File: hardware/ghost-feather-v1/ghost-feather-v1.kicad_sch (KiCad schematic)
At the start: 66 parts, among them J1 Conn_ARM_SWD_TagConnect_TC2030, J2 USB_C_Receptacle_USB2.0, J3 Conn_01x03, J4 Conn_01x03, J5 Conn_01x03, J6 Conn_01x03, J7 Conn_01x08, Q1 BSS138, Q2 BSS138, Q3 BSS138, Q4 BSS138, SW2 BOOT0, U1 STM32F722RETx, U2 BMI270, U3 USBLC6-2SC6_MOD, U4 LM2596S-5, U5 ADP2108AUJ-3.3, X2 32kHz768

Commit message: feat: Assign footprints #1
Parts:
- C1, C10, C11, C12, C14, C15, C16, C17, C3, C4, C5, C6, C7, C9: footprint (none) -> Capacitor_SMD:C_0402_1005Metric
- C13, C2, C8: footprint (none) -> Capacitor_SMD:C_0603_1608Metric
- C18: footprint (none) -> ghost-feather-v1:CAPAE1350X1400N
- L1: footprint (none) -> Inductor_SMD:L_12x12mm_H8mm; Distributor Link (none) -> https://eu.mouser.com/ProductDetail/Coilcraft/MSS1278-333ML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; Manufacturer (none) -> Coilcraft; Manufacturer Part Number (none) -> MSS1278-333MLD
- L2: footprint (none) -> Inductor_SMD:L_0805_2012Metric; Distributor Link (none) -> https://eu.mouser.com/ProductDetail/Murata-Electronics/LQM2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; Manufacturer (none) -> Murata Electronics; Manufacturer Part Number (none) -> LQM21PN1R0MGHL
- U2: footprint BMI270_BOS -> ghost-feather-v1:BMI270_BOS
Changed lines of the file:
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@@
       (effects (font (size 1.27 1.27)) (justify right))
     )
-    (property "Footprint" "" (at 298.45 82.55 0)
+    (property "Footprint" "Capacitor_SMD:C_0402_1005Metric" (at 298.45 82.55 0)
       (effects (font (size 1.27 1.27)) hide)
     )
@@
       (effects (font (size 1.27 1.27)) (justify left))
     )
-    (property "Footprint" "" (at 173.99 171.45 0)
+    (property "Footprint" "Capacitor_SMD:C_0402_1005Metric" (at 173.99 171.45 0)
       (effects (font (size 1.27 1.27)) hide)
     )
@@
       (effects (font (size 1.27 1.27)))
     )
-    (property "Footprint" "" (at 137.16 59.69 0)
+    (property "Footprint" "Inductor_SMD:L_12x12mm_H8mm" (at 137.16 59.69 0)
       (effects (font (size 1.27 1.27)) hide)
     )
@@
       (effects (font (size 1.27 1.27)) hide)
     )
-    (property "Distributor Link" "" (at 137.16 59.69 0)
-      (effects (font (size 1.27 1.27)) hide)
-    )
-    (property "Manufacturer" "" (at 137.16 59.69 0)
-      (effects (font (size 1.27 1.27)) hide)
-    )
-    (property "Manufacturer Part Number" "" (at 137.16 59.69 0)
+    (property "Distributor Link" "https://eu.mouser.com/ProductDetail/Coilcraft/MSS1278-333MLD?qs=zCSbvcPd3pbln1ZLcloB%252BQ%3D%3D" (at 137.16 59.69 0)
+      (effects (font (size 1.27 1.27)) hide)
+    )
+    (property "Manufacturer" "Coilcraft" (at 137.16 59.69 0)
+      (effects (font (size 1.27 1.27)) hide)
+    )
+    (property "Manufacturer Part Number" "MSS1278-333MLD" (at 137.16 59.69 0)
       (effects (font (size 1.27 1.27)) hide)
     )
@@
       (effects (font (size 1.27 1.27)) (justify left))
     )
-    (property "Footprint" "" (at 173.99 191.77 0)
+    (property "Footprint" "Capacitor_SMD:C_0402_1005Metric" (at 173.99 191.77 0)
       (effects (font (size 1.27 1.27)) hide)
     )
@@
       (effects (font (size 1.27 1.27)))
     )
-    (property "Footprint" "" (at 325.12 158.75 0)
+    (property "Footprint" "Capacitor_SMD:C_0402_1005Metric" (at 325.12 158.75 0)
       (effects (font (size 1.27 1.27)) hide)
     )
@@
       (effects (font (size 1.27 1.27)))
     )
-    (property "Footprint" "" (at 203.2 54.61 0)
+    (property "Footprint" "Inductor_SMD:L_0805_2012Metric" (at 203.2 54.61 0)
       (effects (font (size 1.27 1.27)) hide)
     )
@@
       (effects (font (size 1.27 1.27)) hide)
     )
-    (property "Distributor Link" "" (at 203.2 54.61 0)
-      (effects (font (size 1.27 1.27)) hide)
-    )
-    (property "Manufacturer" "" (at 203.2 54.61 0)
-      (effects (font (size 1.27 1.27)) hide)
-    )
-    (property "Manufacturer Part Number" "" (at 203.2 54.61 0)
+    (property "Distributor Link" "https://eu.mouser.com/ProductDetail/Murata-Electronics/LQM21PN1R0MGHL?qs=wM4AZDOQ8I7w4EcrzQRq0A%3D%3D" (at 203.2 54.61 0)
+      (effects (font (size 1.27 1.27)) hide)
+    )
+    (property "Manufacturer" "Murata Electronics" (at 203.2 54.61 0)
+      (effects (font (size 1.27 1.27)) hide)
+    )
+    (property "Manufacturer Part Number" "LQM21PN1R0MGHL" (at 203.2 54.61 0)
       (effects (font (size 1.27 1.27)) hide)
     )
@@
       (effects (font (size 1.27 1.27)) (justify right))
     )
-    (property "Footprint" "" (at 328.93 82.55 0)
+    (property "Footprint" "Capacitor_SMD:C_0402_1005Metric" (at 328.93 82.55 0)
       (effects (font (size 1.27 1.27)) hide)
     )
@@
       (effects (font (size 1.27 1.27)))
     )
-    (property "Footprint" "" (at 325.12 151.13 0)
+    (property "Footprint" "Capacitor_SMD:C_0402_1005Metric" (at 325.12 151.13 0)
       (effects (font (size 1.27 1.27)) hide)
     )
@@
       (effects (font (size 1.27 1.27)) (justify right))
     )
-    (property "Footprint" "" (at 318.77 82.55 0)
+    (property "Footprint" "Capacitor_SMD:C_0402_1005Metric" (at 318.77 82.55 0)
       (effects (font (size 1.27 1.27)) hide)
     )
@@
       (effects (font (size 1.524 1.524)))
     )
-    (property "Footprint" "BMI270_BOS" (at 186.69 91.44 0)
+    (property "Footprint" "ghost-feather-v1:BMI270_BOS" (at 186.69 91.44 0)
       (effects (font (size 1.27 1.27) italic) hide)
     )
@@
       (effects (font (size 1.27 1.27)) (justify right))
     )
-    (property "Footprint" "" (at 257.81 82.55 0)
+    (property "Footprint" "Capacitor_SMD:C_0603_1608Metric" (at 257.81 82.55 0)
       (effects (font (size 1.27 1.27)) hide)
     )
@@
       (effects (font (size 1.27 1.27)) (justify left))
     )
-    (property "Footprint" "" (at 83.82 58.42 0)
+    (property "Footprint" "ghost-feather-v1:CAPAE1350X1400N" (at 83.82 58.42 0)
       (effects (font (size 1.27 1.27)) hide)
     )
@@
       (effects (font (size 1.27 1.27)) (justify left))
     )
-    (property "Footprint" "" (at 173.99 232.41 0)
+    (property "Footprint" "Capacitor_SMD:C_0402_1005Metric" (at 173.99 232.41 0)
       (effects (font (size 1.27 1.27)) hide)
     )
@@
       (effects (font (size 1.27 1.27)) (justify left))
     )
-    (property "Footprint" "" (at 298.45 165.1 0)
+    (property "Footprint" "Capacitor_SMD:C_0603_1608Metric" (at 298.45 165.1 0)
       (effects (font (size 1.27 1.27)) hide)
     )
@@
       (effects (font (size 1.27 1.27)) (justify right))
     )
-    (property "Footprint" "" (at 288.29 82.55 0)
+    (property "Footprint" "Capacitor_SMD:C_0402_1005Metric" (at 288.29 82.55 0)
       (effects (font (size 1.27 1.27)) hide)
     )
@@
       (effects (font (size 1.27 1.27)) (justify left))
     )
-    (property "Footprint" "" (at 308.61 93.98 0)
+    (property "Footprint" "Capacitor_SMD:C_0402_1005Metric" (at 308.61 93.98 0)
       (effects (font (size 1.27 1.27)) hide)
     )
@@
       (effects (font (size 1.27 1.27)) (justify right))
     )
-    (property "Footprint" "" (at 308.61 82.55 0)
+    (property "Footprint" "Capacitor_SMD:C_0402_1005Metric" (at 308.61 82.55 0)
       (effects (font (size 1.27 1.27)) hide)
     )
@@
       (effects (font (size 1.27 1.27)) (justify left))
     )
-    (property "Footprint" "" (at 328.93 124.46 0)
+    (property "Footprint" "Capacitor_SMD:C_0402_1005Metric" (at 328.93 124.46 0)
       (effects (font (size 1.27 1.27)) hide)
     )
@@
       (effects (font (size 1.27 1.27)) (justify left))
     )
-    (property "Footprint" "" (at 173.99 212.09 0)
+    (property "Footprint" "Capacitor_SMD:C_0402_1005Metric" (at 173.99 212.09 0)
       (effects (font (size 1.27 1.27)) hide)
     )
@@
       (effects (font (size 1.27 1.27)) (justify right))
     )
-    (property "Footprint" "" (at 247.65 82.55 0)
+    (property "Footprint" "Capacitor_SMD:C_0402_1005Metric" (at 247.65 82.55 0)
       (effects (font (size 1.27 1.27)) hide)
     )
@@
       (effects (font (size 1.27 1.27)) (justify left))
     )
-    (property "Footprint" "" (at 339.09 82.55 0)
-      (effects (font (size 1.27 1.27)) hide)
-    )
+    (property "Footprint" "Capacitor_SMD:C_0603_1608Metric" (at 339.09 82.55 0)
+      (effects (font (size 1.27 1.27)) hide)
+    )

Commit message: feat: Assign footprints #2
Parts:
- C18: Distributor Link (none) -> https://eu.mouser.com/ProductDetail/Panasonic/EEV-TG1E681UQ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; Manufacturer (none) -> Panasonic; Manufacturer Part Number (none) -> EEV-TG1E681UQ
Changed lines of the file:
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@@
       (effects (font (size 1.27 1.27)) hide)
     )
-    (property "Distributor Link" "" (at 83.82 58.42 0)
+    (property "Distributor Link" "https://eu.mouser.com/ProductDetail/Panasonic/EEV-TG1E681UQ?qs=ojrz6ACP3aSUXVuxdGK87w%3D%3D" (at 83.82 58.42 0)
       (effects (font (size 1.27 1.27)) hide)
     )
-    (property "Manufacturer" "" (at 83.82 58.42 0)
+    (property "Manufacturer" "Panasonic" (at 83.82 58.42 0)
       (effects (font (size 1.27 1.27)) hide)
     )
-    (property "Manufacturer Part Number" "" (at 83.82 58.42 0)
+    (property "Manufacturer Part Number" "EEV-TG1E681UQ" (at 83.82 58.42 0)
       (effects (font (size 1.27 1.27)) hide)
     )

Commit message: feat: Assign footprints #3
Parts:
- D1: footprint (none) -> LED_SMD:LED_0402_1005Metric; Distributor Link (none) -> https://eu.mouser.com/ProductDetail/ROHM-Semiconductor/SML-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; Manufacturer (none) -> ROHM Semiconductor; Manufacturer Part Number (none) -> SML-P11VTT86R
- J2, SW2: footprint (none) -> Connector_USB:USB_C_Receptacle_GCT_USB4085
- J3, J4, J5, J6: footprint (none) -> Connector_Molex:Molex_PicoBlade_53048-0310_1x03_P1.25mm_Horizontal; Distributor Link (none) -> https://eu.mouser.com/ProductDetail/Molex/53048-0310?qs=zXr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; Manufacturer (none) -> Molex; Manufacturer Part Number (none) -> 53048-0310
- J7: footprint (none) -> Connector_Molex:Molex_PicoBlade_53048-0810_1x08_P1.25mm_Horizontal; Distributor Link (none) -> https://eu.mouser.com/ProductDetail/Molex/53048-0810?qs=KHt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; Manufacturer (none) -> Molex; Manufacturer Part Number (none) -> 53048-0810
- R1, R10, R11, R12, R13, R14, R15, R16, R17, R18, R19, R2, R20, R3, R4, R5, R6, R7, R8, R9: footprint (none) -> Resistor_SMD:R_0402_1005Metric

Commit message: feat: Assign footprints #4
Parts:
- D3, D4: footprint (none) -> LED_SMD:LED_0402_1005Metric
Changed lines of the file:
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@@
       (effects (font (size 1.27 1.27)) (justify right))
     )
-    (property "Footprint" "" (at 157.48 64.77 90)
+    (property "Footprint" "LED_SMD:LED_0402_1005Metric" (at 157.48 64.77 90)
       (effects (font (size 1.27 1.27)) hide)
     )
@@
       (effects (font (size 1.27 1.27)) (justify right))
     )
-    (property "Footprint" "" (at 231.14 60.96 90)
-      (effects (font (size 1.27 1.27)) hide)
-    )
+    (property "Footprint" "LED_SMD:LED_0402_1005Metric" (at 231.14 60.96 90)
+      (effects (font (size 1.27 1.27)) hide)
+    )

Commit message: feat: Assign footprints #5
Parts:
- C1: footprint Capacitor_SMD:C_0402_1005Metric -> Capacitor_SMD:C_0603_1608Metric
- C19: footprint (none) -> Capacitor_SMD:C_Elec_10x10.2; Distributor Link (none) -> https://eu.mouser.com/ProductDetail/Panasonic/EEE-TG1V221UP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; Manufacturer (none) -> Panasonic; Manufacturer Part Number (none) -> EEE-TG1V221UP
- C20, C21: footprint (none) -> Capacitor_SMD:C_0603_1608Metric
- D2: footprint (none) -> Diode_SMD:D_SMA; Distributor Link (none) -> https://eu.mouser.com/ProductDetail/Panjit/SBA540AFC_R1_006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; Manufacturer (none) -> Panjit; Manufacturer Part Number (none) -> SBA540AFC_R1_00601
- X1: value ~ -> 16MHz
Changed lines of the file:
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@@
       (effects (font (size 1.27 1.27)) (justify left))
     )
-    (property "Footprint" "" (at 170.18 59.69 0)
+    (property "Footprint" "Capacitor_SMD:C_0603_1608Metric" (at 170.18 59.69 0)
       (effects (font (size 1.27 1.27)) hide)
     )
@@
       (effects (font (size 1.27 1.27)) (justify right))
     )
-    (property "Value" "~" (at 328.93 106.68 0)
+    (property "Value" "16MHz" (at 334.01 106.68 90)
       (effects (font (size 1.27 1.27)))
     )
@@
       (effects (font (size 1.27 1.27)) (justify left))
     )
-    (property "Footprint" "" (at 143.51 63.5 0)
+    (property "Footprint" "Capacitor_SMD:C_Elec_10x10.2" (at 143.51 63.5 0)
       (effects (font (size 1.27 1.27)) hide)
     )
@@
       (effects (font (size 1.27 1.27)) hide)
     )
-    (property "Distributor Link" "" (at 143.51 63.5 0)
-      (effects (font (size 1.27 1.27)) hide)
-    )
-    (property "Manufacturer" "" (at 143.51 63.5 0)
-      (effects (font (size 1.27 1.27)) hide)
-    )
-    (property "Manufacturer Part Number" "" (at 143.51 63.5 0)
+    (property "Distributor Link" "https://eu.mouser.com/ProductDetail/Panasonic/EEE-TG1V221UP?qs=aAAGLDy8P2yKQplSCJZJ1Q%3D%3D" (at 143.51 63.5 0)
+      (effects (font (size 1.27 1.27)) hide)
+    )
+    (property "Manufacturer" "Panasonic" (at 143.51 63.5 0)
+      (effects (font (size 1.27 1.27)) hide)
+    )
+    (property "Manufacturer Part Number" "EEE-TG1V221UP" (at 143.51 63.5 0)
       (effects (font (size 1.27 1.27)) hide)
     )
@@
       (effects (font (size 1.27 1.27)) (justify left))
     )
-    (property "Footprint" "" (at 213.36 60.96 0)
+    (property "Footprint" "Capacitor_SMD:C_0603_1608Metric" (at 213.36 60.96 0)
       (effects (font (size 1.27 1.27)) hide)
     )
@@
       (effects (font (size 1.27 1.27)) (justify right))
     )
-    (property "Footprint" "Capacitor_SMD:C_0402_1005Metric" (at 247.65 82.55 0)
+    (property "Footprint" "Capacitor_SMD:C_0603_1608Metric" (at 247.65 82.55 0)
       (effects (font (size 1.27 1.27)) hide)
     )
@@
       (effects (font (size 1.27 1.27)) (justify left) hide)
     )
-    (property "Footprint" "" (at 130.81 63.5 90)
+    (property "Footprint" "Diode_SMD:D_SMA" (at 130.81 63.5 90)
       (effects (font (size 1.27 1.27)) hide)
     )
@@
       (effects (font (size 1.27 1.27)) hide)
     )
-    (property "Distributor Link" "" (at 130.81 63.5 0)
-      (effects (font (size 1.27 1.27)) hide)
-    )
-    (property "Manufacturer" "" (at 130.81 63.5 0)
-      (effects (font (size 1.27 1.27)) hide)
-    )
-    (property "Manufacturer Part Number" "" (at 130.81 63.5 0)
-      (effects (font (size 1.27 1.27)) hide)
-    )
+    (property "Distributor Link" "https://eu.mouser.com/ProductDetail/Panjit/SBA540AFC_R1_00601?qs=%252BHhoWzUJg4IRjukP4zTDNQ%3D%3D" (at 130.81 63.5 0)
+      (effects (font (size 1.27 1.27)) hide)
+    )
+    (property "Manufacturer" "Panjit" (at 130.81 63.5 0)
+      (effects (font (size 1.27 1.27)) hide)
+    )
+    (property "Manufacturer Part Number" "SBA540AFC_R1_00601" (at 130.81 63.5 0)
+      (effects (font (size 1.27 1.27)) hide)
+    )

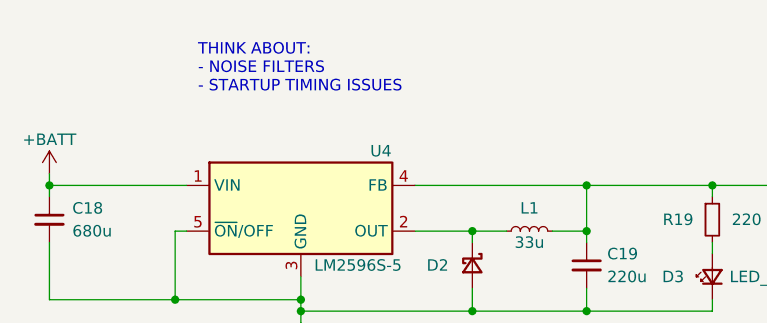
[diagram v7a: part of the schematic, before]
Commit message: feat: Add PMIC related note
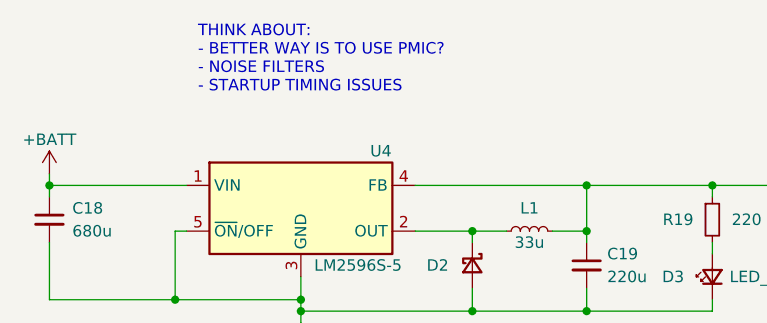
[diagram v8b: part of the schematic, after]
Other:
- note added: "THINK ABOUT: - BETTER WAY IS TO USE PMIC? - NOISE FILTERS - STARTUP TIMING ISSUES"
- note removed: "THINK ABOUT: - NOISE FILTERS - STARTUP TIMING ISSUES"
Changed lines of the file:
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@@
     (stroke (width 0) (type default))
   )
-  (text "THINK ABOUT:\n- NOISE FILTERS\n- STARTUP TIMING ISSUES"
+  (text "THINK ABOUT:\n- BETTER WAY IS TO USE PMIC?\n- NOISE FILTERS\n- STARTUP TIMING ISSUES"
     (at 100.33 44.45 0)
     (effects (font (size 1.27 1.27)) (justify left bottom))
